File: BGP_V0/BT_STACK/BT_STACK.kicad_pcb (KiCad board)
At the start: 2 copper layers, 30 x 30 mm, 13 parts, among them P1 CONN_01X05, U1 OPA180

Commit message: V_0 Updates for caps, gerbers updated
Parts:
- C1: footprint Capacitors_Tantalum_SMD:TantalC_SizeB_EIA-3528_HandSoldering -> Capacitors_SMD:C_0805_HandSoldering
- moved C5 0.21 mm to (176.2, 74.0)
- moved C1 0.07 mm to (184.9, 89.3)
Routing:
- net /V+: track 8.14 -> 13.7 mm, vias 2 -> 1
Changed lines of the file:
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@@
     (thickness 1.6)
     (drawings 9)
-    (tracks 82)
+    (tracks 83)
     (zones 0)
     (modules 13)
@@
     )
   )
-  (module Capacitors_SMD:C_0805_HandSoldering (layer F.Cu)
-    (at 176 74 270)
-    (descr "Capacitor SMD 0805, hand soldering")
-    (tags "capacitor 0805")
-    (attr smd)
-    (fp_text reference C5 (at 1.8 1.5 270) (layer F.SilkS)
-      (effects (font (size 0.6 0.6) (thickness 0.15)))
-    )
-    (fp_text value 0.1u (at -1.3 1.5 270) (layer F.Fab) hide
-      (effects (font (size 0.6 0.6) (thickness 0.15)))
-    )
-    (fp_line (start -2.3 -1) (end 2.3 -1) (layer F.CrtYd) (width 0.05))
-    (fp_line (start -2.3 1) (end 2.3 1) (layer F.CrtYd) (width 0.05))
-    (fp_line (start -2.3 -1) (end -2.3 1) (layer F.CrtYd) (width 0.05))
-    (fp_line (start 2.3 -1) (end 2.3 1) (layer F.CrtYd) (width 0.05))
-    (fp_line (start 0.5 -0.85) (end -0.5 -0.85) (layer F.SilkS) (width 0.15))
-    (fp_line (start -0.5 0.85) (end 0.5 0.85) (layer F.SilkS) (width 0.15))
-    (pad 1 smd rect (at -1.25 0 270) (size 1.5 1.25) (layers F.Cu F.Paste F.Mask)
-      (net 7 /B+))
-    (pad 2 smd rect (at 1.25 0 270) (size 1.5 1.25) (layers F.Cu F.Paste F.Mask)
-      (net 8 /B-))
-    (model Capacitors_SMD.3dshapes/C_0805_HandSoldering.wrl
-      (at (xyz 0 0 0))
-      (scale (xyz 1 1 1))
-      (rotate (xyz 0 0 0))
-    )
-  )
   (module Resistors_SMD:R_0603_HandSoldering (layer F.Cu)
     (at 197 74 270)
@@
       (scale (xyz 1 1 1))
       (rotate (xyz 0 0 0))
-    )
-  )
-  (module Capacitors_Tantalum_SMD:TantalC_SizeB_EIA-3528_HandSoldering (layer B.Cu)
-    (at 184.9 89.3 180)
-    (descr "Tantal Cap. , Size B, EIA-3528, Hand Soldering,")
-    (tags "Tantal Cap. , Size B, EIA-3528, Hand Soldering,")
-    (attr smd)
-    (fp_text reference C1 (at -2.1 2.4 180) (layer B.SilkS)
-      (effects (font (size 0.6 0.6) (thickness 0.15)) (justify mirror))
-    )
-    (fp_text value 22u (at -0.09906 -3.59918 180) (layer B.Fab) hide
-      (effects (font (size 0.6 0.6) (thickness 0.15)) (justify mirror))
-    )
-    (fp_text user + (at -4.70154 2.4003 180) (layer B.SilkS)
-      (effects (font (size 0.6 0.6) (thickness 0.15)) (justify mirror))
-    )
-    (fp_line (start -4.20116 1.89992) (end -4.20116 -1.89992) (layer B.SilkS) (width 0.15))
-    (fp_line (start 2.49936 1.89992) (end -2.49936 1.89992) (layer B.SilkS) (width 0.15))
-    (fp_line (start 2.49682 -1.89992) (end -2.5019 -1.89992) (layer B.SilkS) (width 0.15))
-    (fp_line (start -4.70408 2.90322) (end -4.70408 1.8034) (layer B.SilkS) (width 0.15))
-    (fp_line (start -5.30352 2.40284) (end -4.10464 2.40284) (layer B.SilkS) (width 0.15))
-    (pad 2 smd rect (at 2.12598 0 180) (size 3.1496 1.80086) (layers B.Cu B.Paste B.Mask)
-      (net 2 Earth))
-    (pad 1 smd rect (at -2.12598 0 180) (size 3.1496 1.80086) (layers B.Cu B.Paste B.Mask)
-      (net 1 /V+))
-    (model Capacitors_Tantalum_SMD.3dshapes/TantalC_SizeB_EIA-3528_HandSoldering.wrl
-      (at (xyz 0 0 0))
-      (scale (xyz 1 1 1))
-      (rotate (xyz 0 0 180))
     )
   )
@@
     )
   )
+  (module Capacitors_SMD:C_0805_HandSoldering (layer B.Cu)
+    (at 184.95 89.35 180)
+    (descr "Capacitor SMD 0805, hand soldering")
+    (tags "capacitor 0805")
+    (attr smd)
+    (fp_text reference C1 (at -1.9 1.375001 180) (layer B.SilkS)
+      (effects (font (size 0.6 0.6) (thickness 0.15)) (justify mirror))
+    )
+    (fp_text value 22u (at 0 -2.1 180) (layer B.Fab) hide
+      (effects (font (size 0.6 0.6) (thickness 0.15)) (justify mirror))
+    )
+    (fp_line (start -2.3 1) (end 2.3 1) (layer B.CrtYd) (width 0.05))
+    (fp_line (start -2.3 -1) (end 2.3 -1) (layer B.CrtYd) (width 0.05))
+    (fp_line (start -2.3 1) (end -2.3 -1) (layer B.CrtYd) (width 0.05))
+    (fp_line (start 2.3 1) (end 2.3 -1) (layer B.CrtYd) (width 0.05))
+    (fp_line (start 0.5 0.85) (end -0.5 0.85) (layer B.SilkS) (width 0.15))
+    (fp_line (start -0.5 -0.85) (end 0.5 -0.85) (layer B.SilkS) (width 0.15))
+    (pad 1 smd rect (at -1.25 0 180) (size 1.5 1.25) (layers B.Cu B.Paste B.Mask)
+      (net 1 /V+))
+    (pad 2 smd rect (at 1.25 0 180) (size 1.5 1.25) (layers B.Cu B.Paste B.Mask)
+      (net 2 Earth))
+    (model Capacitors_SMD.3dshapes/C_0805_HandSoldering.wrl
+      (at (xyz 0 0 0))
+      (scale (xyz 1 1 1))
+      (rotate (xyz 0 0 0))
+    )
+  )
+  (module Capacitors_SMD:C_0805_HandSoldering (layer F.Cu)
+    (at 176.2 73.95 270)
+    (descr "Capacitor SMD 0805, hand soldering")
+    (tags "capacitor 0805")
+    (attr smd)
+    (fp_text reference C5 (at 1.75 1.4 270) (layer F.SilkS)
+      (effects (font (size 0.6 0.6) (thickness 0.15)))
+    )
+    (fp_text value 0.1u (at 0 2.1 270) (layer F.Fab) hide
+      (effects (font (size 0.6 0.6) (thickness 0.15)))
+    )
+    (fp_line (start -2.3 -1) (end 2.3 -1) (layer F.CrtYd) (width 0.05))
+    (fp_line (start -2.3 1) (end 2.3 1) (layer F.CrtYd) (width 0.05))
+    (fp_line (start -2.3 -1) (end -2.3 1) (layer F.CrtYd) (width 0.05))
+    (fp_line (start 2.3 -1) (end 2.3 1) (layer F.CrtYd) (width 0.05))
+    (fp_line (start 0.5 -0.85) (end -0.5 -0.85) (layer F.SilkS) (width 0.15))
+    (fp_line (start -0.5 0.85) (end 0.5 0.85) (layer F.SilkS) (width 0.15))
+    (pad 1 smd rect (at -1.25 0 270) (size 1.5 1.25) (layers F.Cu F.Paste F.Mask)
+      (net 7 /B+))
+    (pad 2 smd rect (at 1.25 0 270) (size 1.5 1.25) (layers F.Cu F.Paste F.Mask)
+      (net 8 /B-))
+    (model Capacitors_SMD.3dshapes/C_0805_HandSoldering.wrl
+      (at (xyz 0 0 0))
+      (scale (xyz 1 1 1))
+      (rotate (xyz 0 0 0))
+    )
+  )
   (gr_text "BGP V0.0\nB/T Stack" (at 196 70) (layer B.SilkS)
     (effects (font (size 0.6 0.6) (thickness 0.15)) (justify mirror))
@@
   (gr_line (start 170 68) (end 170 98) (angle 90) (layer Edge.Cuts) (width 0.15))
   (gr_line (start 200 68) (end 170 68) (angle 90) (layer Edge.Cuts) (width 0.15))
-  (via (at 188 84.1) (size 0.6) (layers F.Cu B.Cu) (net 1))
-  (via (at 187.6 91.6) (size 0.6) (layers F.Cu B.Cu) (net 1))
-  (segment (start 187.026 85.074) (end 188 84.1) (width 0.5) (layer B.Cu) (net 1))
-  (segment (start 187.026 89.3) (end 187.026 85.074) (width 0.5) (layer B.Cu) (net 1))
-  (segment (start 187.026 91.026) (end 187.6 91.6) (width 0.5) (layer B.Cu) (net 1))
-  (segment (start 187.026 89.3) (end 187.026 91.026) (width 0.5) (layer B.Cu) (net 1))
+  (segment (start 187.9 84.1) (end 186.4 84.1) (width 0.5) (layer F.Cu) (net 1))
+  (segment (start 186.4 84.1) (end 186.35 84.05) (width 0.5) (layer F.Cu) (net 1))
+  (segment (start 186.2 89.35) (end 186.2 85.8) (width 0.5) (layer B.Cu) (net 1))
+  (segment (start 186.2 85.8) (end 187.9 84.1) (width 0.5) (layer B.Cu) (net 1))
+  (via (at 187.9 84.1) (size 0.6) (drill 0.4) (layers F.Cu B.Cu) (net 1))
+  (segment (start 187 95.2) (end 187 90.15) (width 0.5) (layer B.Cu) (net 1))
+  (segment (start 187 90.15) (end 186.2 89.35) (width 0.5) (layer B.Cu) (net 1))
   (via (at 181.876 85.7452) (size 0.6) (layers F.Cu B.Cu) (net 2))
   (segment (start 182.32 85.3015) (end 181.876 85.7452) (width 0.5) (layer F.Cu) (net 2))

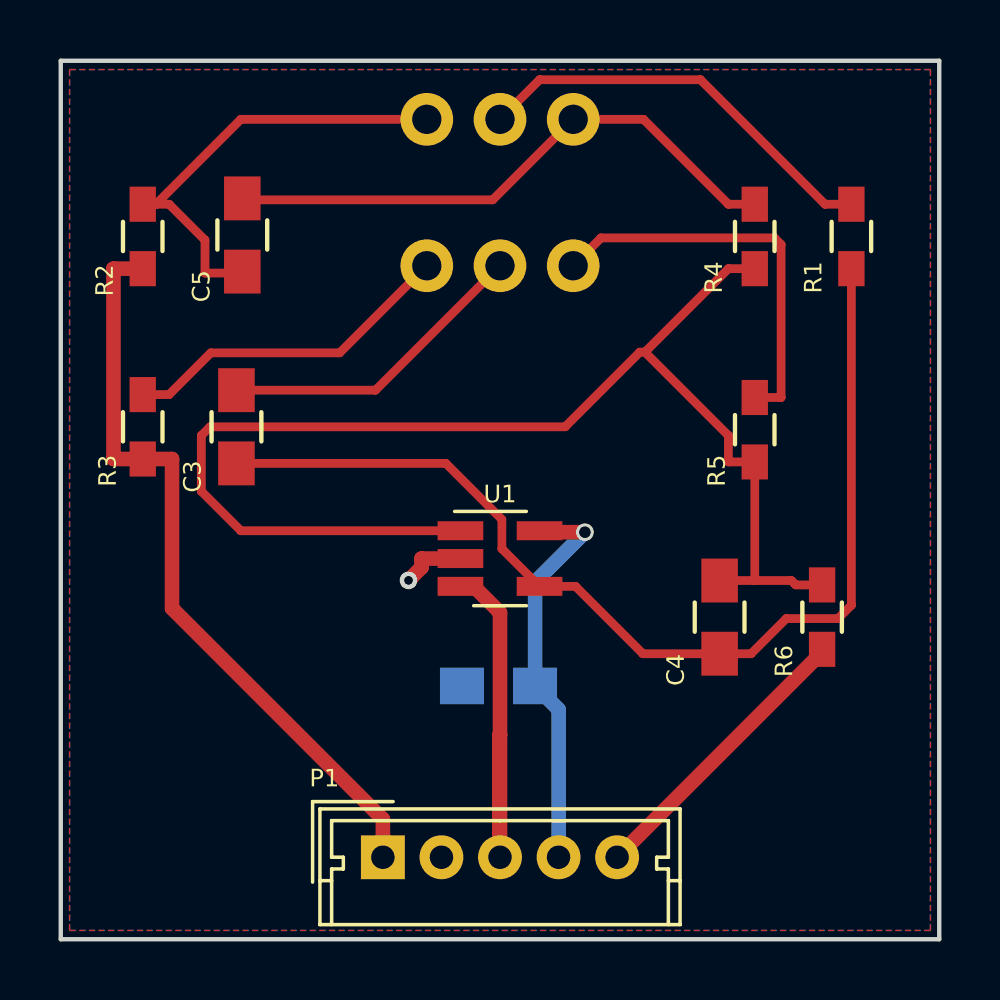
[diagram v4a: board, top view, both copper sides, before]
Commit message: V0 BUF and BT Edits
V0 Buffer change from CRD to JFET CCS. BT stack changed to reflect +/- 9V changes.
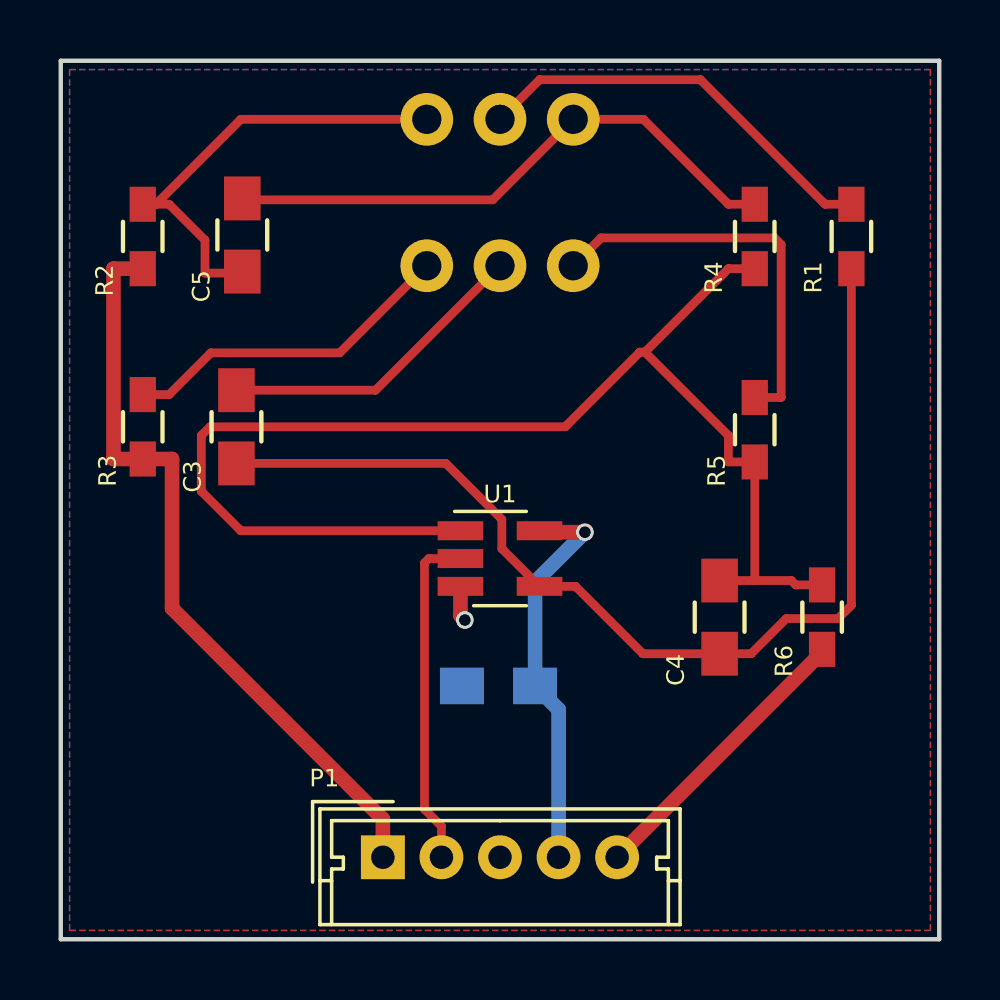
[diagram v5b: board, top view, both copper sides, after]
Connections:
- C1 pad 2: Earth -> Net-(C1-Pad2)
- P1 pad 2: Earth -> /V-
- P1 pad 3: /REF -> Earth
- U1 pad 2: Earth -> /V-
- U1 pad 3: /REF -> Earth
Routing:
- net /REF: track 14.3 -> 0.00 mm
- net /V-: track 0.00 -> 11.6 mm
- net Earth: track 2.26 -> 1.21 mm
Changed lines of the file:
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@@
-(kicad_pcb (version 4) (host pcbnew 4.0.4-1.fc24-product)
+(kicad_pcb (version 4) (host pcbnew 4.0.7)
   (general
-    (links 23)
+    (links 22)
     (no_connects 0)
     (area 169.924999 67.424999 200.075001 99.455)
     (thickness 1.6)
     (drawings 9)
-    (tracks 83)
+    (tracks 80)
     (zones 0)
     (modules 13)
-    (nets 14)
+    (nets 15)
   )
   (page A4)
@@
   (net 7 /B+)
   (net 8 /B-)
-  (net 9 /REF)
-  (net 10 /OUT)
-  (net 11 /BW)
-  (net 12 /T-)
-  (net 13 /T+)
+  (net 9 /OUT)
+  (net 10 /BW)
+  (net 11 /T-)
+  (net 12 /T+)
+  (net 13 "Net-(C1-Pad2)")
+  (net 14 /V-)
   (net_class Default "This is the default net class."
     (clearance 0.3)
@@
     (add_net /T-)
     (add_net /TW)
+    (add_net /V-)
+    (add_net "Net-(C1-Pad2)")
     (add_net "Net-(C3-Pad2)")
     (add_net "Net-(C4-Pad1)")
@@
     (add_net /IN)
     (add_net /OUT)
-    (add_net /REF)
     (add_net /V+)
     (add_net Earth)
@@
       (net 6 "Net-(C4-Pad1)"))
     (pad 2 smd rect (at -1.35 0) (size 1.56 0.65) (layers F.Cu F.Paste F.Mask)
+      (net 14 /V-))
+    (pad 3 smd rect (at -1.35 0.95) (size 1.56 0.65) (layers F.Cu F.Paste F.Mask)
       (net 2 Earth))
-    (pad 3 smd rect (at -1.35 0.95) (size 1.56 0.65) (layers F.Cu F.Paste F.Mask)
-      (net 9 /REF))
     (pad 4 smd rect (at 1.35 0.95) (size 1.56 0.65) (layers F.Cu F.Paste F.Mask)
       (net 5 "Net-(C3-Pad2)"))
@@
     (fp_line (start -0.5 -0.675) (end 0.5 -0.675) (layer F.SilkS) (width 0.15))
     (pad 1 smd rect (at -1.1 0 270) (size 1.2 0.9) (layers F.Cu F.Paste F.Mask)
-      (net 11 /BW))
+      (net 10 /BW))
     (pad 2 smd rect (at 1.1 0 270) (size 1.2 0.9) (layers F.Cu F.Paste F.Mask)
       (net 5 "Net-(C3-Pad2)"))
@@
     (fp_line (start -0.5 -0.675) (end 0.5 -0.675) (layer F.SilkS) (width 0.15))
     (pad 1 smd rect (at -1.1 0 270) (size 1.2 0.9) (layers F.Cu F.Paste F.Mask)
-      (net 12 /T-))
+      (net 11 /T-))
     (pad 2 smd rect (at 1.1 0 270) (size 1.2 0.9) (layers F.Cu F.Paste F.Mask)
       (net 3 /IN))
@@
       (net 6 "Net-(C4-Pad1)"))
     (pad 2 smd rect (at 1.1 0 90) (size 1.2 0.9) (layers F.Cu F.Paste F.Mask)
-      (net 13 /T+))
+      (net 12 /T+))
     (model Resistors_SMD.3dshapes/R_0603_HandSoldering.wrl
       (at (xyz 0 0 0))
@@
     (fp_line (start -0.5 -0.675) (end 0.5 -0.675) (layer F.SilkS) (width 0.15))
     (pad 1 smd rect (at -1.1 0 90) (size 1.2 0.9) (layers F.Cu F.Paste F.Mask)
-      (net 10 /OUT))
+      (net 9 /OUT))
     (pad 2 smd rect (at 1.1 0 90) (size 1.2 0.9) (layers F.Cu F.Paste F.Mask)
       (net 6 "Net-(C4-Pad1)"))
@@
       (net 3 /IN))
     (pad 2 thru_hole circle (at 2 0) (size 1.5 1.5) (drill 0.8) (layers *.Cu *.Mask)
+      (net 14 /V-))
+    (pad 3 thru_hole circle (at 4 0) (size 1.5 1.5) (drill 0.8) (layers *.Cu *.Mask)
       (net 2 Earth))
-    (pad 3 thru_hole circle (at 4 0) (size 1.5 1.5) (drill 0.8) (layers *.Cu *.Mask)
-      (net 9 /REF))
     (pad 4 thru_hole circle (at 6 0) (size 1.5 1.5) (drill 0.8) (layers *.Cu *.Mask)
       (net 1 /V+))
     (pad 5 thru_hole circle (at 8 0) (size 1.5 1.5) (drill 0.8) (layers *.Cu *.Mask)
-      (net 10 /OUT))
+      (net 9 /OUT))
     (model ${KISYS3DMOD}/Connectors_Molex.3dshapes/Molex_MicroLatch-53253-0570_05x2.00mm_Straight.wrl
       (at (xyz 0 0 0))
@@
       (net 7 /B+))
     (pad 2 thru_hole circle (at 0 2.5 90) (size 1.8 1.8) (drill 1) (layers *.Cu *.Mask)
-      (net 11 /BW))
+      (net 10 /BW))
     (pad 1 thru_hole circle (at 0 0 90) (size 1.8 1.8) (drill 1) (layers *.Cu *.Mask)
       (net 8 /B-))
     (pad 6 thru_hole circle (at -5 5 90) (size 1.8 1.8) (drill 1) (layers *.Cu *.Mask)
-      (net 13 /T+))
+      (net 12 /T+))
     (pad 5 thru_hole circle (at -5 2.5 90) (size 1.8 1.8) (drill 1) (layers *.Cu *.Mask)
       (net 4 /TW))
     (pad 4 thru_hole circle (at -5 0 90) (size 1.8 1.8) (drill 1) (layers *.Cu *.Mask)
-      (net 12 /T-))
+      (net 11 /T-))
     (model Potentiometers.3dshapes/Potentiometer_Alps_RK097_Double_Vertical.wrl
       (at (xyz 0 0 0))
@@
       (net 1 /V+))
     (pad 2 smd rect (at 1.25 0 180) (size 1.5 1.25) (layers B.Cu B.Paste B.Mask)
-      (net 2 Earth))
+      (net 13 "Net-(C1-Pad2)"))
     (model Capacitors_SMD.3dshapes/C_0805_HandSoldering.wrl
       (at (xyz 0 0 0))
@@
   (segment (start 187 95.2) (end 187 90.15) (width 0.5) (layer B.Cu) (net 1))
   (segment (start 187 90.15) (end 186.2 89.35) (width 0.5) (layer B.Cu) (net 1))
-  (via (at 181.876 85.7452) (size 0.6) (layers F.Cu B.Cu) (net 2))
-  (segment (start 182.32 85.3015) (end 181.876 85.7452) (width 0.5) (layer F.Cu) (net 2))
-  (segment (start 182.32 85) (end 182.32 85.3015) (width 0.5) (layer F.Cu) (net 2))
-  (segment (start 183.65 85) (end 182.32 85) (width 0.5) (layer F.Cu) (net 2))
+  (segment (start 183.65 85.95) (end 183.65 86.95) (width 0.5) (layer F.Cu) (net 2))
+  (via (at 183.8 87.1) (size 0.6) (drill 0.4) (layers F.Cu B.Cu) (net 2))
+  (segment (start 183.65 86.95) (end 183.8 87.1) (width 0.5) (layer F.Cu) (net 2))
   (segment (start 171.7997 81.6) (end 171.7997 75.1) (width 0.5) (layer F.Cu) (net 3))
   (segment (start 172.8 81.6) (end 171.7997 81.6) (width 0.5) (layer F.Cu) (net 3))
@@
   (segment (start 176.15 70) (end 182.5 70) (width 0.3) (layer F.Cu) (net 8))
   (segment (start 173.25 72.9) (end 176.15 70) (width 0.3) (layer F.Cu) (net 8))
-  (segment (start 184.6 95.1) (end 184.98 94.7197) (width 0.5) (layer F.Cu) (net 9))
-  (segment (start 185 95.2) (end 185 91.0225) (width 0.5) (layer F.Cu) (net 9))
-  (segment (start 184.105 85.95) (end 183.65 85.95) (width 0.5) (layer F.Cu) (net 9))
-  (segment (start 185 86.845) (end 184.105 85.95) (width 0.5) (layer F.Cu) (net 9))
-  (segment (start 185 91.0225) (end 185 86.845) (width 0.5) (layer F.Cu) (net 9))
-  (segment (start 184.98 91.0425) (end 184.98 94.7197) (width 0.5) (layer F.Cu) (net 9))
-  (segment (start 185 91.0225) (end 184.98 91.0425) (width 0.5) (layer F.Cu) (net 9))
-  (segment (start 196 88.2) (end 196 88.1) (width 0.5) (layer F.Cu) (net 10))
-  (segment (start 189 95.2) (end 196 88.2) (width 0.5) (layer F.Cu) (net 10))
-  (segment (start 191.8465 68.6468) (end 196.0997 72.9) (width 0.3) (layer F.Cu) (net 11))
-  (segment (start 186.3532 68.6468) (end 191.8465 68.6468) (width 0.3) (layer F.Cu) (net 11))
-  (segment (start 185 70) (end 186.3532 68.6468) (width 0.3) (layer F.Cu) (net 11))
-  (segment (start 197 72.9) (end 196.0997 72.9) (width 0.3) (layer F.Cu) (net 11))
-  (segment (start 175.1253 77.975) (end 173.7003 79.4) (width 0.3) (layer F.Cu) (net 12))
-  (segment (start 179.525 77.975) (end 175.1253 77.975) (width 0.3) (layer F.Cu) (net 12))
-  (segment (start 182.5 75) (end 179.525 77.975) (width 0.3) (layer F.Cu) (net 12))
-  (segment (start 172.8 79.4) (end 173.7003 79.4) (width 0.3) (layer F.Cu) (net 12))
-  (segment (start 194.6003 74.2745) (end 194.6003 79.5) (width 0.3) (layer F.Cu) (net 13))
-  (segment (start 194.3754 74.0496) (end 194.6003 74.2745) (width 0.3) (layer F.Cu) (net 13))
-  (segment (start 188.4504 74.0496) (end 194.3754 74.0496) (width 0.3) (layer F.Cu) (net 13))
-  (segment (start 187.5 75) (end 188.4504 74.0496) (width 0.3) (layer F.Cu) (net 13))
-  (segment (start 193.7 79.5) (end 194.6003 79.5) (width 0.3) (layer F.Cu) (net 13))
+  (segment (start 196 88.2) (end 196 88.1) (width 0.5) (layer F.Cu) (net 9))
+  (segment (start 189 95.2) (end 196 88.2) (width 0.5) (layer F.Cu) (net 9))
+  (segment (start 191.8465 68.6468) (end 196.0997 72.9) (width 0.3) (layer F.Cu) (net 10))
+  (segment (start 186.3532 68.6468) (end 191.8465 68.6468) (width 0.3) (layer F.Cu) (net 10))
+  (segment (start 185 70) (end 186.3532 68.6468) (width 0.3) (layer F.Cu) (net 10))
+  (segment (start 197 72.9) (end 196.0997 72.9) (width 0.3) (layer F.Cu) (net 10))
+  (segment (start 175.1253 77.975) (end 173.7003 79.4) (width 0.3) (layer F.Cu) (net 11))
+  (segment (start 179.525 77.975) (end 175.1253 77.975) (width 0.3) (layer F.Cu) (net 11))
+  (segment (start 182.5 75) (end 179.525 77.975) (width 0.3) (layer F.Cu) (net 11))
+  (segment (start 172.8 79.4) (end 173.7003 79.4) (width 0.3) (layer F.Cu) (net 11))
+  (segment (start 194.6003 74.2745) (end 194.6003 79.5) (width 0.3) (layer F.Cu) (net 12))
+  (segment (start 194.3754 74.0496) (end 194.6003 74.2745) (width 0.3) (layer F.Cu) (net 12))
+  (segment (start 188.4504 74.0496) (end 194.3754 74.0496) (width 0.3) (layer F.Cu) (net 12))
+  (segment (start 187.5 75) (end 188.4504 74.0496) (width 0.3) (layer F.Cu) (net 12))
+  (segment (start 193.7 79.5) (end 194.6003 79.5) (width 0.3) (layer F.Cu) (net 12))
+  (segment (start 183.65 85) (end 182.57 85) (width 0.3) (layer F.Cu) (net 14))
+  (segment (start 182.57 85) (end 182.419999 85.150001) (width 0.3) (layer F.Cu) (net 14))
+  (segment (start 182.419999 85.150001) (end 182.419999 93.559339) (width 0.3) (layer F.Cu) (net 14))
+  (segment (start 182.419999 93.559339) (end 183 94.13934) (width 0.3) (layer F.Cu) (net 14))
+  (segment (start 183 94.13934) (end 183 95.2) (width 0.3) (layer F.Cu) (net 14))
   (zone (net 2) (net_name Earth) (layer B.Cu) (hatch edge 0.508)
     (connect_pads (clearance 0.3))
